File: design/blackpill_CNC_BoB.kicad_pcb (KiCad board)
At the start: 4 copper layers, 298 parts, among them J101 ALimIN, J102 ZLimIN, J103 YLimIN, J104 XLimIN, J105 CS_IN, J106 FH_IN, J107 DoorIN, J108 ResetIN, J109 ProbeIN, J110 12V Power in, J111 AuxEncIn, J112 5V Power out, J113 ADC_in_1, J114 ADC_in_2, J115 stepDriverLim, J116 Reset, J117 UART1, J118 I2C, J119 SpindleVFD, J120 Spindle/Coolant, J121 Spindle, J122 Coolant, J123 AuxOut, J124 XStepDrv, J125 YStepDrv, J126 ZStepDrv, J127 AStepDrv, U101 TLP290-4, U102 TLP290-4, U103 TLP290-4, U104 74LVC2G17, U105 LD1117S50TR_SOT223, U106 LM358, U107 TLV9001, U108 TLV9001, U109 YAAJ_WeAct_BlackPill_Part_Like, U110 TLV9001, U111 TLV9001, U112 74HCT541, U113 74HCT541, U114 74HCT541, U115 ULN2003A, U116 ULN2003A, U117 ULN2003A

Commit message: change screw terminals and start placing analog in
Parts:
- added D120: 1N5819, Diode_SMD:D_SOD-323, F.Cu at (59.6, -10.5)
- added JP238: Jumper_NC_Dual, Connector_PinHeader_2.54mm:PinHeader_1x03_P2.54mm_Vertical, F.Cu at (55.2, -9.60)
- J101, J102, J103, J104, J105, J106, J107, J108, J109, J113, J114: footprint Connector_Phoenix_MSTB:PhoenixContact_MSTBA_2,5_2-G-5,08_1x02_P5.08mm_Horizontal -> conn_my_kf128:ScrewTerminal_1x2_P2.54mm_Vertical
- J111: footprint Connector_PinHeader_2.00mm:PinHeader_1x04_P2.00mm_Vertical -> Connector_PinSocket_2.54mm:PinSocket_1x04_P2.54mm_Vertical
- J119, J121, J122, J123, J124, J125, J126, J127: footprint Connector_Phoenix_MSTB:PhoenixContact_MSTBA_2,5_4-G-5,08_1x04_P5.08mm_Horizontal -> conn_my_kf128:ScrewTerminal_1x4_P2.54mm_Vertical
- moved R135 274.6 mm to (219.7, 129.5)
- moved R129 217.9 mm to (201.9, 125.7)
- moved JP170 203.9 mm to (54.6, 121.9), turned to 180 degrees
- moved JP166 201.5 mm to (71.1, 121.9), turned to 180 degrees
- moved R134 197.0 mm to (217.2, 157.5)
- moved R125 194.9 mm to (191.8, 142.2)
- moved JP168 191.3 mm to (48.3, 121.9), turned to 180 degrees
- moved JP165 190.2 mm to (68.6, 121.9), turned to 180 degrees
- moved R136 188.9 mm to (222.2, 157.5)
- moved U110 185.0 mm to (224.8, 132.1)
- moved R131 182.4 mm to (207.0, 125.7)
- moved JP169 182.3 mm to (50.8, 121.9), turned to 180 degrees
- moved JP106 182.2 mm to (200.7, 175.3), turned to 180 degrees
- moved JP167 181.1 mm to (45.7, 121.9), turned to 180 degrees
- moved JP163 180.1 mm to (63.5, 121.9), turned to 180 degrees
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- renumbered d90 to D115, r90 to R167
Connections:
- C110 pad 1: Net-(C110-Pad1) -> /UADCdriver
- C113 pad 1: Net-(C110-Pad1) -> /UADCdriver
- JP112 pad 2: Net-(C110-Pad1) -> /UADCdriver
- U109 pad 18: +5V -> /U5uC
- U109 pad 38: +5V -> /U5uC

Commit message: place buffer cercos
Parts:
- added C124: 100nF, Capacitor_SMD:C_0603_1608Metric, F.Cu at (208.3, 134.6)
- added C125: 100nF, Capacitor_SMD:C_0603_1608Metric, F.Cu at (85.1, 94.0)
- added C126: 100nF, Capacitor_SMD:C_0603_1608Metric, F.Cu at (230.6, 143.5)
- moved RV101 251.4 mm to (214.6, 147.3)
- moved C108 239.9 mm to (25.4, 99.1), turned to 180 degrees
- moved C109 233.8 mm to (53.3, 99.1), turned to 180 degrees
- moved JP172 231.2 mm to (228.6, 135.9)
- moved JP113 206.2 mm to (210.8, 138.4)
- moved JP140 204.5 mm to (221.0, 135.9)
- moved C110 201.7 mm to (231.1, 154.9)
- moved C116 193.5 mm to (175.3, 80.0), turned to 270 degrees
- moved JP173 187.1 mm to (231.1, 166.4)
- moved C114 180.7 mm to (213.4, 142.2)
- moved D105 177.6 mm to (219.7, 125.7)
- moved C120 176.1 mm to (226.1, 137.2)
- moved D104 175.7 mm to (210.8, 156.2)
- moved C112 168.6 mm to (207.0, 167.6)
- moved D108 168.3 mm to (226.1, 153.7)
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
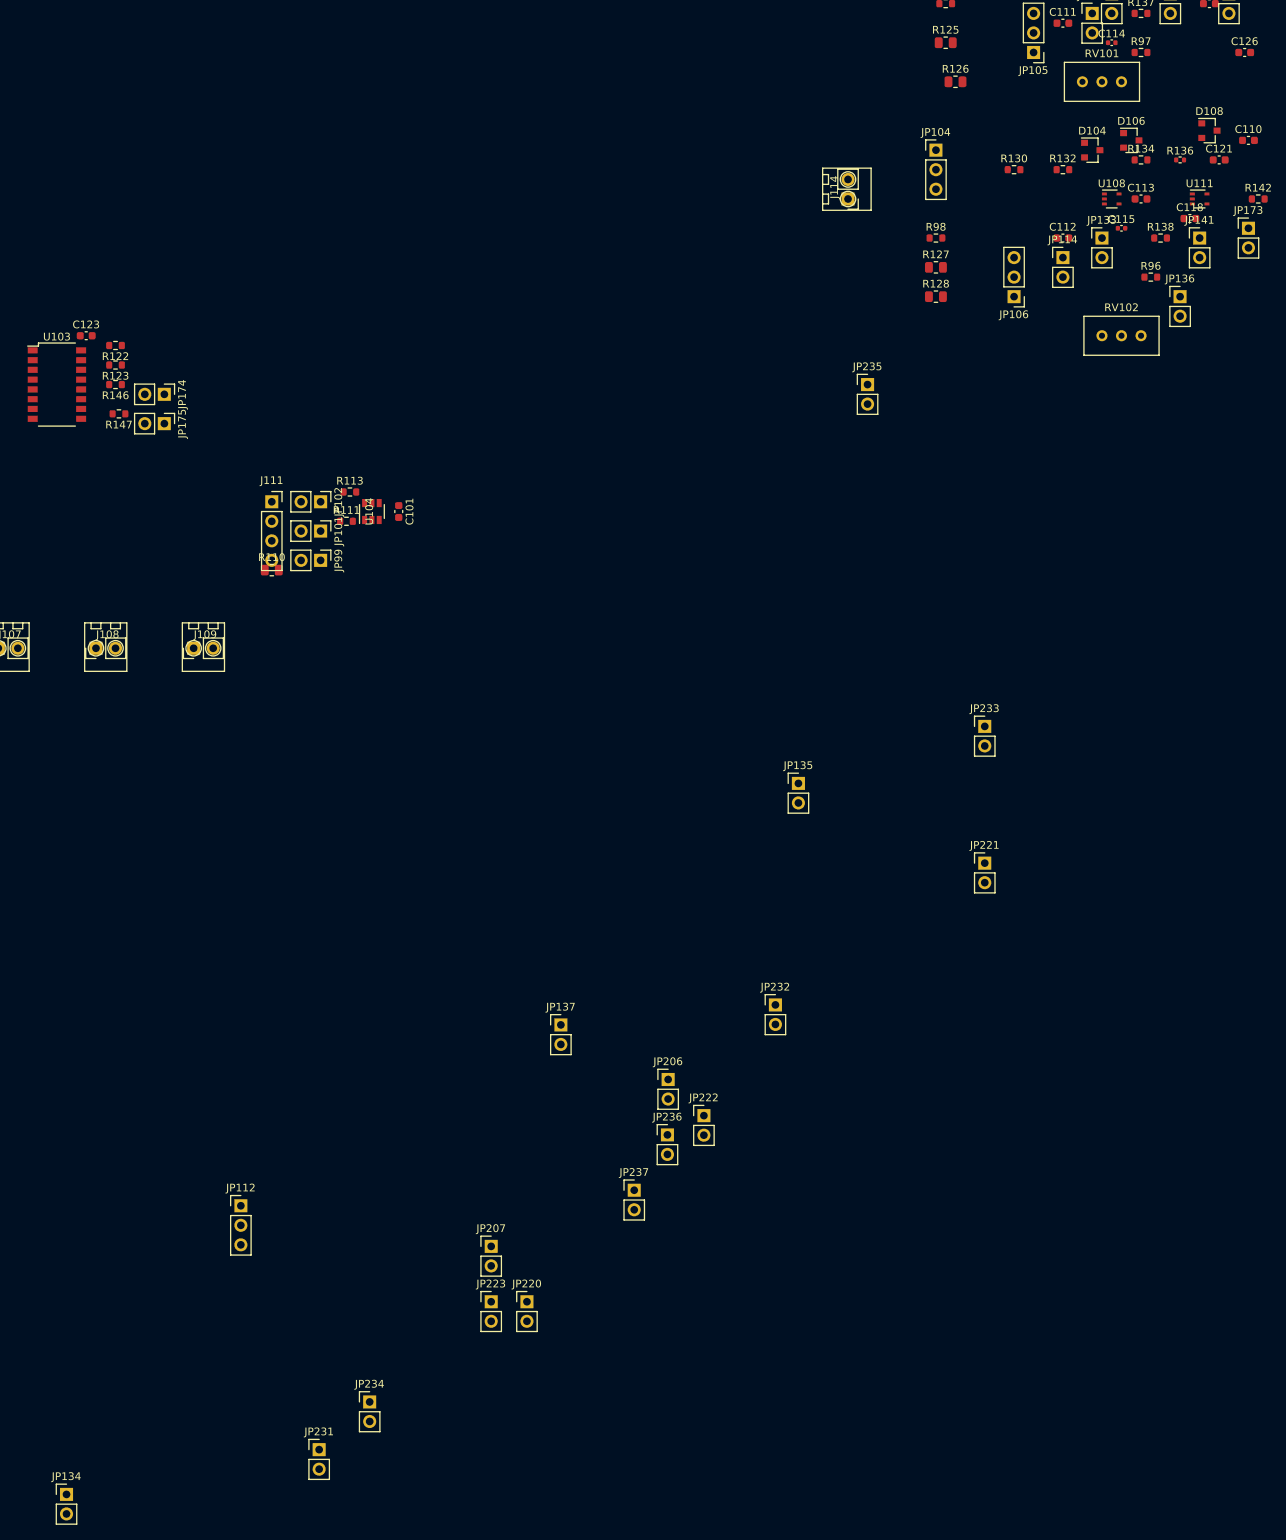
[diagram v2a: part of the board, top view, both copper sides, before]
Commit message: refigure AD in jumper
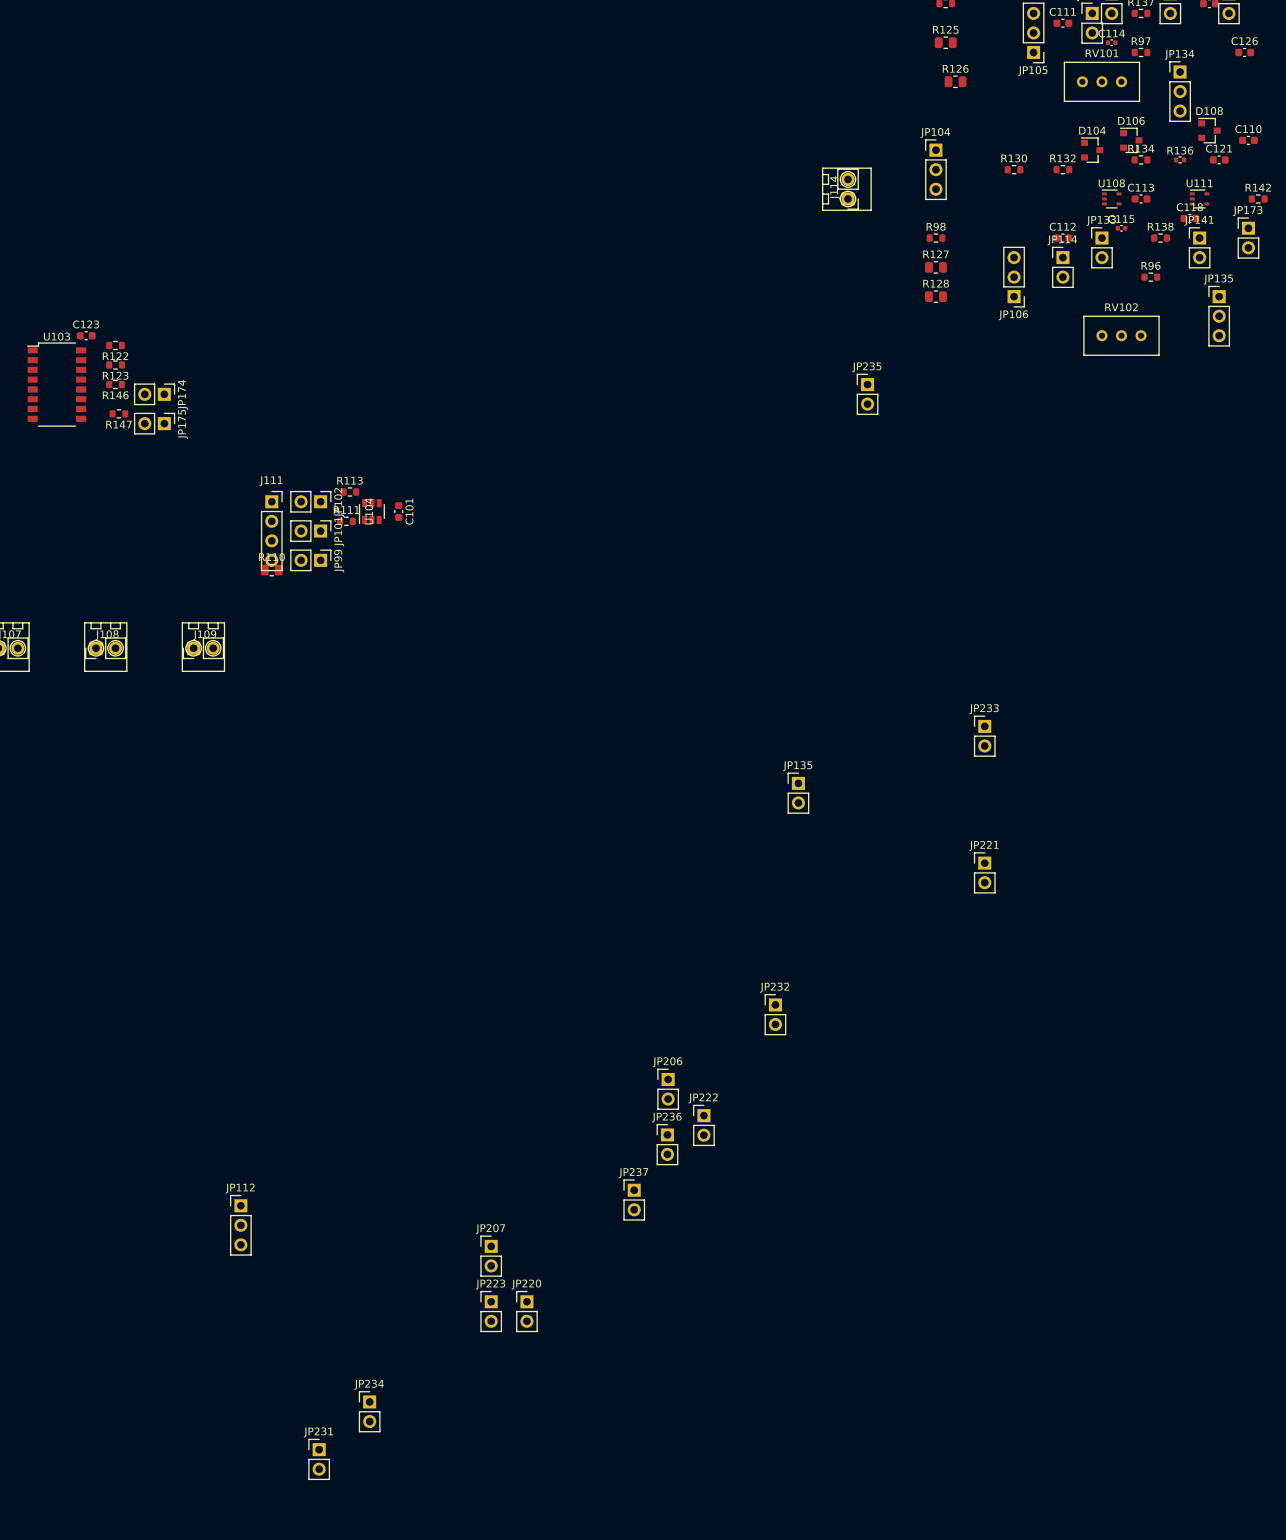
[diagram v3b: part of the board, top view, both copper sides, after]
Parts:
- removed JP136, JP137: Jumper_NC_Small, Connector_PinHeader_2.54mm:PinHeader_1x02_P2.54mm_Vertical
- added JP135: Jumper_NC_Dual, Connector_PinHeader_2.54mm:PinHeader_1x03_P2.54mm_Vertical, F.Cu at (227.3, 175.3)
- JP134: value Jumper_NC_Small -> Jumper_NC_Dual; footprint Connector_PinHeader_2.54mm:PinHeader_1x02_P2.54mm_Vertical -> Connector_PinHeader_2.54mm:PinHeader_1x03_P2.54mm_Vertical
- moved JP134 234.9 mm to (222.2, 146.1)
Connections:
- R134 pad 2: Net-(JP136-Pad1) -> Net-(JP135-Pad1)
- RV101 pad 2: Net-(JP135-Pad1) -> Net-(JP134-Pad3)
- RV102 pad 1: Net-(JP136-Pad1) -> Net-(JP135-Pad1)
- U108 pad 1: Net-(JP136-Pad1) -> Net-(JP135-Pad1)

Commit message: refigure driver voltage jumper
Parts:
- added J128: Driver Power in/out, Connector_Phoenix_MSTB:PhoenixContact_MSTBA_2,5_2-G-5,08_1x02_P5.08mm_Horizontal, F.Cu at (146.1, 27.9)
- added JP136: Jumper_NC_Dual, Connector_PinHeader_2.54mm:PinHeader_1x03_P2.54mm_Vertical, F.Cu at (137.2, 22.9)
- moved JP112 229.9 mm to (123.2, 64.8)
- moved D120 99.4 mm to (118.1, 69.8)
- moved JP238 91.0 mm to (115.6, 58.4)
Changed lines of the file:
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@@
     (tracks 0)
     (zones 0)
-    (modules 302)
+    (modules 304)
     (nets 282)
   )
@@
     (add_net "Net-(JP135-Pad2)")
     (add_net "Net-(JP135-Pad3)")
-    (add_net "Net-(JP136-Pad1)")
-    (add_net "Net-(JP137-Pad1)")
     (add_net "Net-(JP138-Pad2)")
     (add_net "Net-(JP139-Pad2)")
@@
   )
   (module Connector_PinHeader_2.54mm:PinHeader_1x03_P2.54mm_Vertical (layer F.Cu)
+    (at 137.16 22.86 270)
+    (descr "Through hole straight pin header, 1x03, 2.54mm pitch, single row")
+    (tags "Through hole pin header THT 1x03 2.54mm single row")
+    (fp_text reference JP136 (at 0 -2.33 90) (layer F.SilkS)
+      (effects (font (size 1 1) (thickness 0.15)))
+    )
+    (fp_text value Jumper_NC_Dual (at 0 7.41 90) (layer F.Fab)
+      (effects (font (size 1 1) (thickness 0.15)))
+    )
+    (fp_text user %R (at 0 2.54) (layer F.Fab)
+      (effects (font (size 1 1) (thickness 0.15)))
+    )
+    (fp_line (start -0.635 -1.27) (end 1.27 -1.27) (layer F.Fab) (width 0.1))
+    (fp_line (start 1.27 -1.27) (end 1.27 6.35) (layer F.Fab) (width 0.1))
+    (fp_line (start 1.27 6.35) (end -1.27 6.35) (layer F.Fab) (width 0.1))
+    (fp_line (start -1.27 6.35) (end -1.27 -0.635) (layer F.Fab) (width 0.1))
+    (fp_line (start -1.27 -0.635) (end -0.635 -1.27) (layer F.Fab) (width 0.1))
+    (fp_line (start -1.33 6.41) (end 1.33 6.41) (layer F.SilkS) (width 0.12))
+    (fp_line (start -1.33 1.27) (end -1.33 6.41) (layer F.SilkS) (width 0.12))
+    (fp_line (start 1.33 1.27) (end 1.33 6.41) (layer F.SilkS) (width 0.12))
+    (fp_line (start -1.33 1.27) (end 1.33 1.27) (layer F.SilkS) (width 0.12))
+    (fp_line (start -1.33 0) (end -1.33 -1.33) (layer F.SilkS) (width 0.12))
+    (fp_line (start -1.33 -1.33) (end 0 -1.33) (layer F.SilkS) (width 0.12))
+    (fp_line (start -1.8 -1.8) (end -1.8 6.85) (layer F.CrtYd) (width 0.05))
+    (fp_line (start -1.8 6.85) (end 1.8 6.85) (layer F.CrtYd) (width 0.05))
+    (fp_line (start 1.8 6.85) (end 1.8 -1.8) (layer F.CrtYd) (width 0.05))
+    (fp_line (start 1.8 -1.8) (end -1.8 -1.8) (layer F.CrtYd) (width 0.05))
+    (pad 3 thru_hole oval (at 0 5.08 270) (size 1.7 1.7) (drill 1) (layers *.Cu *.Mask)
+      (net 3 +12V))
+    (pad 2 thru_hole oval (at 0 2.54 270) (size 1.7 1.7) (drill 1) (layers *.Cu *.Mask)
+      (net 245 Vdrive))
+    (pad 1 thru_hole rect (at 0 0 270) (size 1.7 1.7) (drill 1) (layers *.Cu *.Mask)
+      (net 1 +5V))
+    (model ${KISYS3DMOD}/Connector_PinHeader_2.54mm.3dshapes/PinHeader_1x03_P2.54mm_Vertical.wrl
+      (at (xyz 0 0 0))
+      (scale (xyz 1 1 1))
+      (rotate (xyz 0 0 0))
+    )
+  )
+  (module Connector_Phoenix_MSTB:PhoenixContact_MSTBA_2,5_2-G-5,08_1x02_P5.08mm_Horizontal (layer F.Cu)
+    (at 146.05 27.94 90)
+    (descr "Generic Phoenix Contact connector footprint for: MSTBA_2,5/2-G-5,08; number of pins: 02; pin pitch: 5.08mm; Angled || order number: 1757242 12A || order number: 1923869 16A (HC)")
+    (tags "phoenix_contact connector MSTBA_01x02_G_5.08mm")
+    (fp_text reference J128 (at 2.54 -3.2 90) (layer F.SilkS)
+      (effects (font (size 1 1) (thickness 0.15)))
+    )
+    (fp_text value "Driver Power in/out" (at 2.54 11.2 90) (layer F.Fab)
+      (effects (font (size 1 1) (thickness 0.15)))
+    )
+    (fp_text user %R (at 2.54 -1.3 90) (layer F.Fab)
+      (effects (font (size 1 1) (thickness 0.15)))
+    )
+    (fp_line (start -3.65 -2.11) (end -3.65 10.11) (layer F.SilkS) (width 0.12))
+    (fp_line (start -3.65 10.11) (end 8.73 10.11) (layer F.SilkS) (width 0.12))
+    (fp_line (start 8.73 10.11) (end 8.73 -2.11) (layer F.SilkS) (width 0.12))
+    (fp_line (start 8.73 -2.11) (end -3.65 -2.11) (layer F.SilkS) (width 0.12))
+    (fp_line (start -3.54 -2) (end -3.54 10) (layer F.Fab) (width 0.1))
+    (fp_line (start -3.54 10) (end 8.62 10) (layer F.Fab) (width 0.1))
+    (fp_line (start 8.62 10) (end 8.62 -2) (layer F.Fab) (width 0.1))
+    (fp_line (start 8.62 -2) (end -3.54 -2) (layer F.Fab) (width 0.1))
+    (fp_line (start -3.65 8.61) (end -3.65 6.81) (layer F.SilkS) (width 0.12))
+    (fp_line (start -3.65 6.81) (end 8.73 6.81) (layer F.SilkS) (width 0.12))
+    (fp_line (start 8.73 6.81) (end 8.73 8.61) (layer F.SilkS) (width 0.12))
+    (fp_line (start 8.73 8.61) (end -3.65 8.61) (layer F.SilkS) (width 0.12))
+    (fp_line (start -1 10.11) (end 1 10.11) (layer F.SilkS) (width 0.12))
+    (fp_line (start 1 10.11) (end 0.75 8.61) (layer F.SilkS) (width 0.12))
+    (fp_line (start 0.75 8.61) (end -0.75 8.61) (layer F.SilkS) (width 0.12))
+    (fp_line (start -0.75 8.61) (end -1 10.11) (layer F.SilkS) (width 0.12))
+    (fp_line (start 4.08 10.11) (end 6.08 10.11) (layer F.SilkS) (width 0.12))
+    (fp_line (start 6.08 10.11) (end 5.83 8.61) (layer F.SilkS) (width 0.12))
+    (fp_line (start 5.83 8.61) (end 4.33 8.61) (layer F.SilkS) (width 0.12))
+    (fp_line (start 4.33 8.61) (end 4.08 10.11) (layer F.SilkS) (width 0.12))
+    (fp_line (start -4.04 -2.5) (end -4.04 10.5) (layer F.CrtYd) (width 0.05))
+    (fp_line (start -4.04 10.5) (end 9.12 10.5) (layer F.CrtYd) (width 0.05))
+    (fp_line (start 9.12 10.5) (end 9.12 -2.5) (layer F.CrtYd) (width 0.05))
+    (fp_line (start 9.12 -2.5) (end -4.04 -2.5) (layer F.CrtYd) (width 0.05))
+    (fp_line (start 0.3 -2.91) (end 0 -2.31) (layer F.SilkS) (width 0.12))
+    (fp_line (start 0 -2.31) (end -0.3 -2.91) (layer F.SilkS) (width 0.12))
+    (fp_line (start -0.3 -2.91) (end 0.3 -2.91) (layer F.SilkS) (width 0.12))
+    (fp_line (start 0.95 -2) (end 0 -0.5) (layer F.Fab) (width 0.1))
+    (fp_line (start 0 -0.5) (end -0.95 -2) (layer F.Fab) (width 0.1))
+    (pad 2 thru_hole oval (at 5.08 0 90) (size 2.08 3.6) (drill 1.4) (layers *.Cu *.Mask)
+      (net 245 Vdrive))
+    (pad 1 thru_hole roundrect (at 0 0 90) (size 2.08 3.6) (drill 1.4) (layers *.Cu *.Mask) (roundrect_rratio 0.120192)
+      (net 2 GND))
+    (model ${KISYS3DMOD}/Connector_Phoenix_MSTB.3dshapes/PhoenixContact_MSTBA_2,5_2-G-5,08_1x02_P5.08mm_Horizontal.wrl
+      (at (xyz 0 0 0))
+      (scale (xyz 1 1 1))
+      (rotate (xyz 0 0 0))
+    )
+  )
+  (module Connector_PinHeader_2.54mm:PinHeader_1x03_P2.54mm_Vertical (layer F.Cu)
     (at 227.33 175.26)
     (descr "Through hole straight pin header, 1x03, 2.54mm pitch, single row")
@@
   )
   (module Connector_PinHeader_2.54mm:PinHeader_1x03_P2.54mm_Vertical (layer F.Cu)
-    (at 55.165001 -9.604999)
+    (at 115.57 58.42)
     (descr "Through hole straight pin header, 1x03, 2.54mm pitch, single row")
     (tags "Through hole pin header THT 1x03 2.54mm single row")
@@
   )
   (module Diode_SMD:D_SOD-323 (layer F.Cu)
-    (at 59.615001 -10.454999)
+    (at 118.11 69.85)
     (descr SOD-323)
     (tags SOD-323)
@@
   )
   (module Connector_PinHeader_2.54mm:PinHeader_1x03_P2.54mm_Vertical (layer F.Cu)
-    (at 100.119001 293.473001)
+    (at 123.19 64.77)
     (descr "Through hole straight pin header, 1x03, 2.54mm pitch, single row")
     (tags "Through hole pin header THT 1x03 2.54mm single row")

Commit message: still ... refigure driver voltage jumper
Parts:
- removed the JP135 at (172.6, 238.6)
- removed JP136: Jumper_NC_Dual, Connector_PinHeader_2.54mm:PinHeader_1x03_P2.54mm_Vertical
- removed REF**: PinHeader_1x04_P2.54mm_Vertical, Connector_PinHeader_2.54mm:PinHeader_1x04_P2.54mm_Vertical
- moved JP234 266.4 mm to (96.5, 53.3), turned to 180 degrees
- moved JP237 252.7 mm to (59.7, 55.9), turned to 180 degrees
- moved JP236 237.7 mm to (99.1, 53.3), turned to 180 degrees
- moved JP232 227.0 mm to (94.0, 53.3), turned to 180 degrees
- moved JP233 225.7 mm to (54.6, 55.9), turned to 180 degrees
- moved JP235 180.6 mm to (57.1, 55.9), turned to 180 degrees
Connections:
- net Vdrive renamed /V_Drive

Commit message: arrange adc in
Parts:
- added J129: Relais Power in/out, conn_my_kf128:ScrewTerminal_1x2_P2.54mm_Vertical, F.Cu at (-20.3, -1.27)
- J112, J128: footprint Connector_Phoenix_MSTB:PhoenixContact_MSTBA_2,5_2-G-5,08_1x02_P5.08mm_Horizontal -> conn_my_kf128:ScrewTerminal_1x2_P2.54mm_Vertical
- moved JP220 280.6 mm to (7.62, 57.1), turned to 180 degrees
- moved JP223 275.1 mm to (15.2, 57.1), turned to 180 degrees
- moved JP231 271.9 mm to (102.9, 53.3), turned to 180 degrees
- moved JP222 268.8 mm to (12.7, 57.1), turned to 180 degrees
- moved JP221 267.6 mm to (10.2, 57.1), turned to 180 degrees
- moved JP207 245.1 mm to (68.6, 62.2)
- moved JP206 218.2 mm to (100.3, 66.0)
- moved J124 54.9 mm to (54.6, -1.27), turned to 0 degrees
- moved J125 45.9 mm to (43.2, -1.27), turned to 0 degrees
- moved J126 38.1 mm to (31.8, -1.27), turned to 0 degrees
- moved J127 32.6 mm to (20.3, -1.27), turned to 0 degrees
- moved C124 26.5 mm to (200.7, 160.0), turned to 90 degrees
- moved R142 24.3 mm to (208.9, 156.2), turned to 270 degrees
- moved JP205 24.3 mm to (-8.89, 57.1)
- moved J123 22.9 mm to (8.89, -1.27), turned to 0 degrees
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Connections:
- C124 pad 1: /UADCdriver -> +5V
- C126 pad 1: /UADCdriver -> +5V

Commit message: align top edge connectors
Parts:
- moved C126 112.6 mm to (118.7, 130.8), turned to 90 degrees
- moved C110 106.9 mm to (127.0, 130.8), turned to 90 degrees
- moved R141 105.6 mm to (127.0, 127.0), turned to 270 degrees
- moved D107 103.5 mm to (123.8, 127.0), turned to 270 degrees
- moved U110 100.3 mm to (124.5, 130.8), turned to 270 degrees
- moved D105 99.7 mm to (120.0, 127.0), turned to 270 degrees
- moved R135 97.8 mm to (121.9, 130.8), turned to 90 degrees
- moved JP172 96.1 mm to (132.7, 128.9)
- moved D103 95.9 mm to (116.2, 127.0), turned to 270 degrees
- moved JP134 95.3 mm to (127.6, 134.6), turned to 270 degrees
- moved R131 94.6 mm to (112.4, 128.3)
- moved C114 94.6 mm to (118.7, 140.3), turned to 180 degrees
- moved JP132 94.6 mm to (118.7, 137.2), turned to 180 degrees
- moved JP113 94.6 mm to (116.2, 137.2), turned to 180 degrees
- moved U107 94.6 mm to (116.2, 130.8), turned to 270 degrees
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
